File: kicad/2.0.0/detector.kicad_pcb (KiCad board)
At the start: 2 copper layers, 67 parts, among them U1 LM317, U2 LM337, U3 REF5010ID, U4 OPA2197xD, U5 OPA2197xD

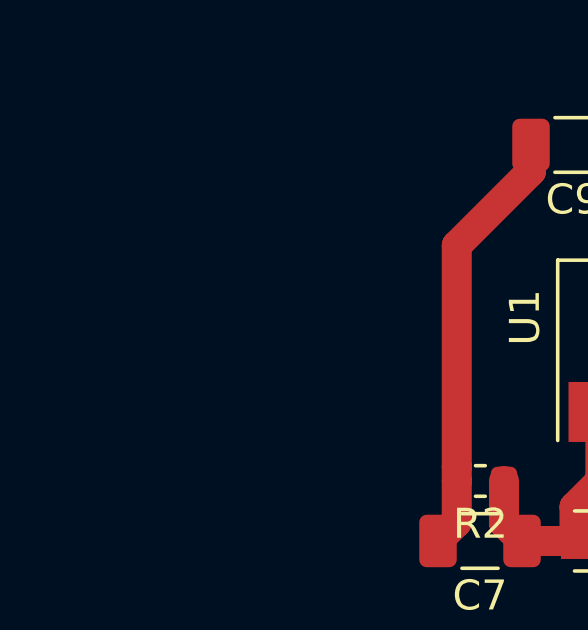
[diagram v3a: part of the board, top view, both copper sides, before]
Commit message: replaced voltage regulators of 2.0.0 detector with LDO regulators
Low-dropout (LDO) voltage regulators come in small packages, i.e.
SOT-23, however they are more susceptible for ringing.
The packages in which you can buy the non-LDO voltage regulators, e.g. SOIC-8 or SOT-223,
are large compared to the remaining circuitry.
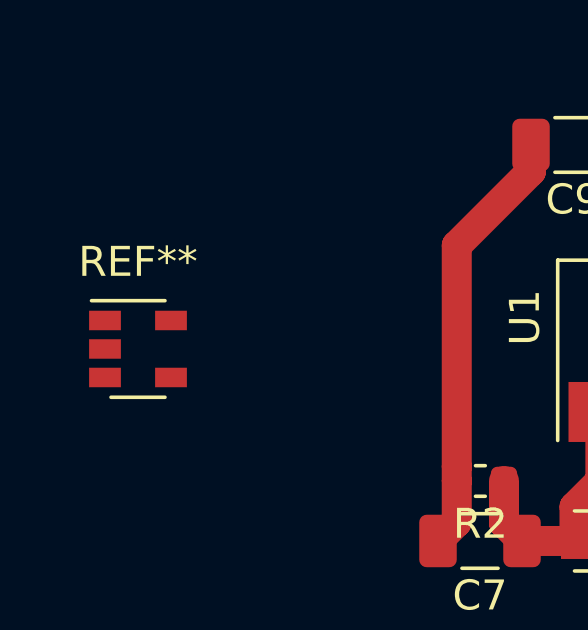
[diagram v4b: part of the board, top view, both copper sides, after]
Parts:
- added REF**: SOT-23-5, Package_TO_SOT_SMD:SOT-23-5, F.Cu at (44.3, 88.2)
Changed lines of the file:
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@@
     (tracks 155)
     (zones 0)
-    (modules 67)
+    (modules 68)
     (nets 25)
   )
@@
     (35 F.Paste user)
     (36 B.SilkS user)
-    (37 F.SilkS user hide)
+    (37 F.SilkS user)
     (38 B.Mask user)
     (39 F.Mask user)
@@
     (47 F.CrtYd user)
     (48 B.Fab user)
-    (49 F.Fab user hide)
+    (49 F.Fab user)
   )
   (setup
@@
     (add_net "Net-(U3-Pad8)")
   )
+  (module Package_TO_SOT_SMD:SOT-23-5 (layer F.Cu)
+    (at 44.3 88.2)
+    (descr "5-pin SOT23 package")
+    (tags SOT-23-5)
+    (attr smd)
+    (fp_text reference REF** (at 0 -2.9) (layer F.SilkS)
+      (effects (font (size 1 1) (thickness 0.15)))
+    )
+    (fp_text value SOT-23-5 (at 0 2.9) (layer F.Fab)
+      (effects (font (size 1 1) (thickness 0.15)))
+    )
+    (fp_line (start 0.9 -1.55) (end 0.9 1.55) (layer F.Fab) (width 0.1))
+    (fp_line (start 0.9 1.55) (end -0.9 1.55) (layer F.Fab) (width 0.1))
+    (fp_line (start -0.9 -0.9) (end -0.9 1.55) (layer F.Fab) (width 0.1))
+    (fp_line (start 0.9 -1.55) (end -0.25 -1.55) (layer F.Fab) (width 0.1))
+    (fp_line (start -0.9 -0.9) (end -0.25 -1.55) (layer F.Fab) (width 0.1))
+    (fp_line (start -1.9 1.8) (end -1.9 -1.8) (layer F.CrtYd) (width 0.05))
+    (fp_line (start 1.9 1.8) (end -1.9 1.8) (layer F.CrtYd) (width 0.05))
+    (fp_line (start 1.9 -1.8) (end 1.9 1.8) (layer F.CrtYd) (width 0.05))
+    (fp_line (start -1.9 -1.8) (end 1.9 -1.8) (layer F.CrtYd) (width 0.05))
+    (fp_line (start 0.9 -1.61) (end -1.55 -1.61) (layer F.SilkS) (width 0.12))
+    (fp_line (start -0.9 1.61) (end 0.9 1.61) (layer F.SilkS) (width 0.12))
+    (fp_text user %R (at 0 0 90) (layer F.Fab)
+      (effects (font (size 0.5 0.5) (thickness 0.075)))
+    )
+    (pad 5 smd rect (at 1.1 -0.95) (size 1.06 0.65) (layers F.Cu F.Paste F.Mask))
+    (pad 4 smd rect (at 1.1 0.95) (size 1.06 0.65) (layers F.Cu F.Paste F.Mask))
+    (pad 3 smd rect (at -1.1 0.95) (size 1.06 0.65) (layers F.Cu F.Paste F.Mask))
+    (pad 2 smd rect (at -1.1 0) (size 1.06 0.65) (layers F.Cu F.Paste F.Mask))
+    (pad 1 smd rect (at -1.1 -0.95) (size 1.06 0.65) (layers F.Cu F.Paste F.Mask))
+    (model ${KISYS3DMOD}/Package_TO_SOT_SMD.3dshapes/SOT-23-5.wrl
+      (at (xyz 0 0 0))
+      (scale (xyz 1 1 1))
+      (rotate (xyz 0 0 0))
+    )
+  )
   (module Capacitor_SMD:C_0603_1608Metric (layer F.Cu)

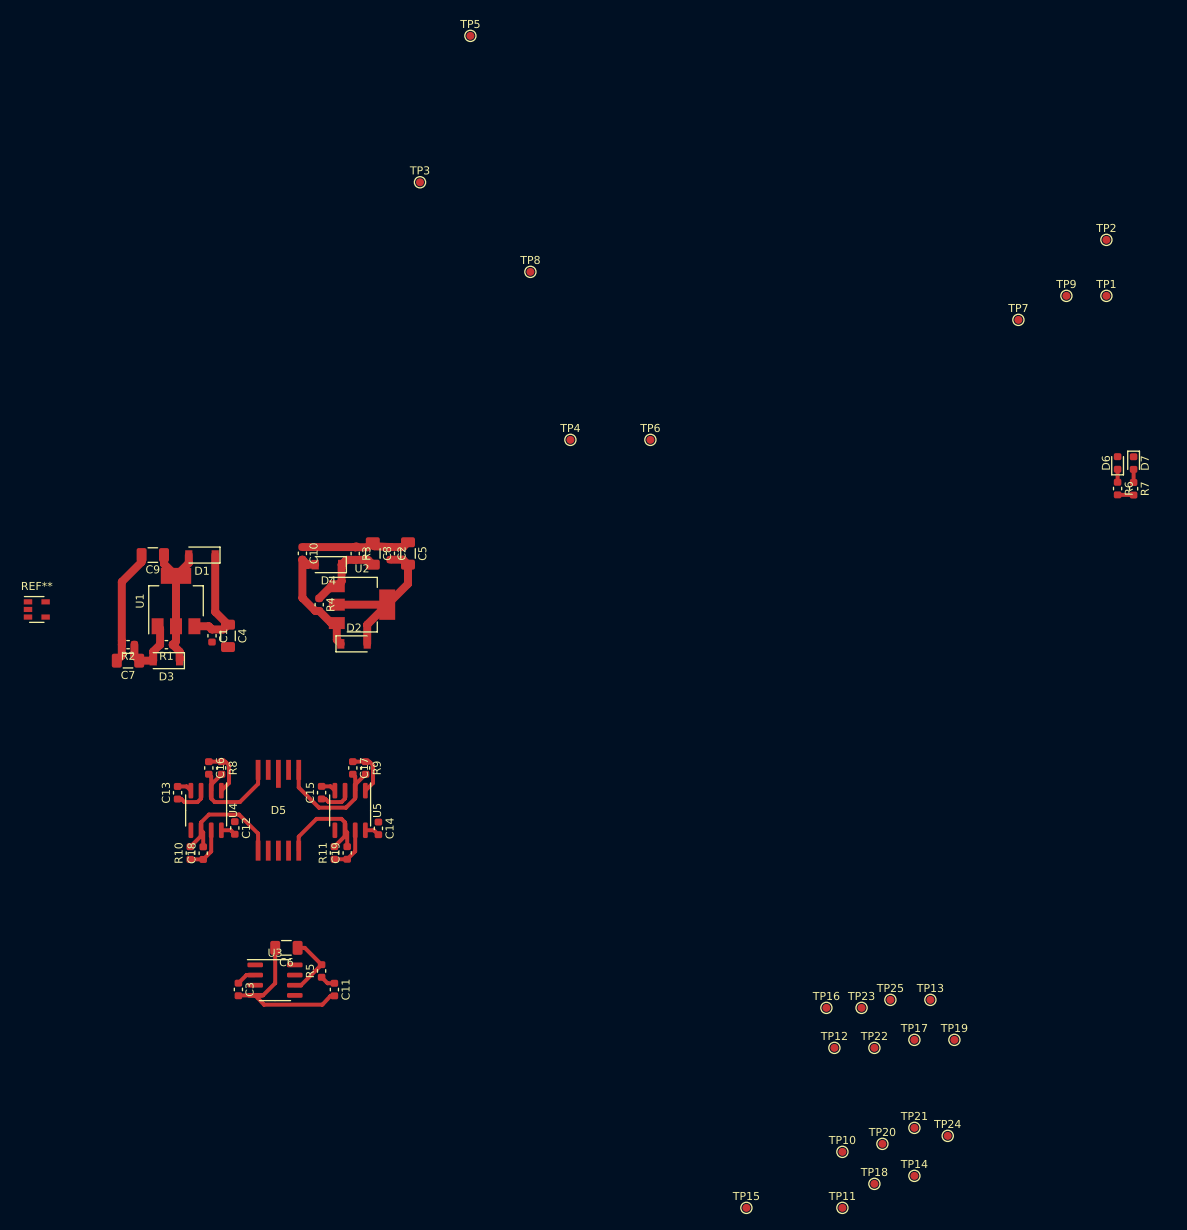
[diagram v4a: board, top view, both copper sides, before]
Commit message: updated pcb of 2.0.0 detector with new power supply
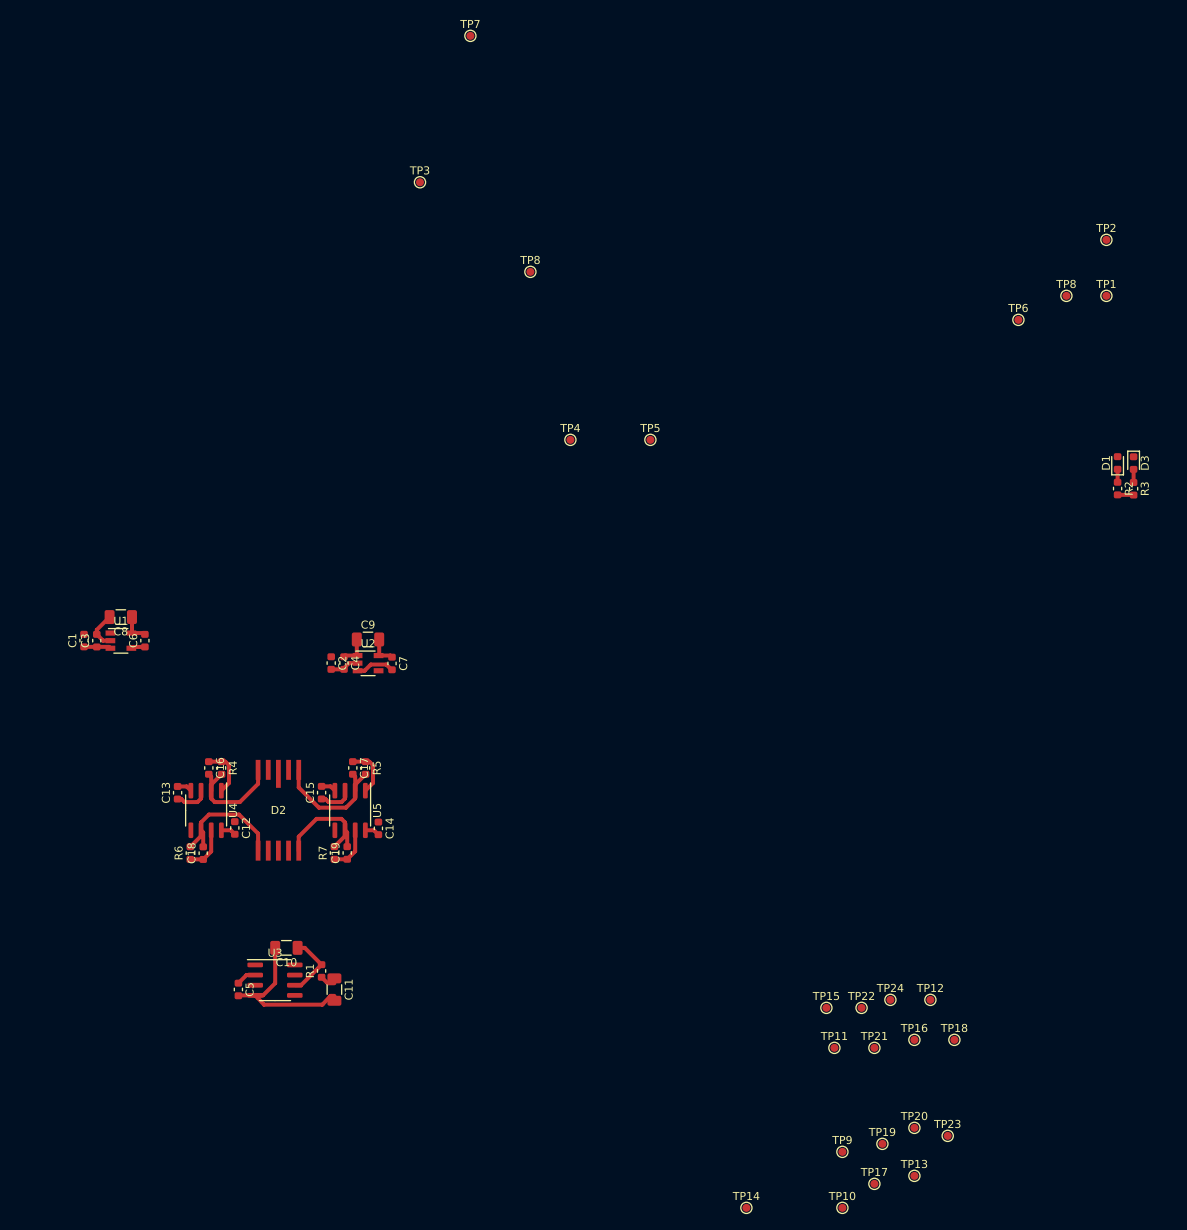
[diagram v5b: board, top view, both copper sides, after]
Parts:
- removed the C10 at (77.5, 81.2)
- removed the C5 at (90.7, 81.2)
- removed the D1 at (65.0, 81.4)
- removed the D2 at (84.0, 92.5)
- removed the D3 at (60.5, 94.6)
- removed D4: D_Small, Diode_SMD:D_SOD-123
- removed the R1 at (60.5, 92.6)
- removed the R2 at (55.7, 92.6)
- removed the R3 at (84.1, 81.2)
- removed the R4 at (79.6, 87.6)
- removed REF**: SOT-23-5, Package_TO_SOT_SMD:SOT-23-5
- added C3: 1u, Capacitor_SMD:C_0603_1608Metric, F.Cu at (51.8, 92.1)
- added C6: 10n, Capacitor_SMD:C_0603_1608Metric, F.Cu at (57.8, 92.1)
- C1, C2: value 10u -> 100n
- C11: footprint Capacitor_SMD:C_0603_1608Metric -> Capacitor_SMD:C_1206_3216Metric
- C4: value 100n -> 1u; footprint Capacitor_SMD:C_1206_3216Metric -> Capacitor_SMD:C_0603_1608Metric
- C7: value 10u -> 10n; footprint Capacitor_SMD:C_1206_3216Metric -> Capacitor_SMD:C_0603_1608Metric
- C8: value 10u -> 22u
- U1: value LM317 -> LT1761-5; footprint Package_TO_SOT_SMD:SOT-223-3_TabPin2 -> Package_TO_SOT_SMD:TSOT-23-5
- U2: value LM337 -> LT1964-5; footprint Package_TO_SOT_SMD:SOT-223-3_TabPin2 -> Package_TO_SOT_SMD:TSOT-23-5
- moved C7 33.0 mm to (88.7, 95.0), turned to 270 degrees
- moved C8 32.5 mm to (54.8, 89.2), turned to 180 degrees
- moved C9 28.9 mm to (85.7, 92.0), turned to 0 degrees
- moved C1 16.0 mm to (50.2, 92.1), turned to 90 degrees
- moved C2 15.6 mm to (81.1, 94.9)
- moved C4 14.9 mm to (82.7, 94.9)
- moved U1 8.48 mm to (54.8, 92.1), turned to 0 degrees
- moved U2 7.35 mm to (85.7, 94.9)
- renumbered C6 to C10, C3 to C5, D6 to D1, D5 to D2, D7 to D3, R5 to R1, R6 to R2, R7 to R3, R8 to R4, R9 to R5, R10 to R6, R11 to R7, TP11 to TP10, TP12 to TP11, TP13 to TP12, TP14 to TP13, TP15 to TP14, TP16 to TP15, TP17 to TP16, TP18 to TP17, TP19 to TP18, TP20 to TP19, TP21 to TP20, TP22 to TP21, TP23 to TP22, TP24 to TP23, TP25 to TP24, TP6 to TP5, TP7 to TP6, TP5 to TP7, TP9 to TP8, TP10 to TP9
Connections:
- C1 pad 2: GND -> Net-(C1-Pad2)
- C2 pad 1: GND -> Net-(C1-Pad2)
- C4 pad 1: +15V -> GND
- C4 pad 2: GND -> -15V
- C7 pad 1: Net-(C7-Pad1) -> -5V
- C7 pad 2: GND -> Net-(C7-Pad2)
- C8 pad 1: GND -> +5V
- C8 pad 2: Net-(C8-Pad2) -> GND
- C9 pad 1: +12V -> GND
- C9 pad 2: GND -> -5V
- TP5 pad 1: +12V -> +5V
- TP6 pad 1: -12V -> -5V
- U1 pad 1: Net-(C7-Pad1) -> +15V
- U1 pad 2: +12V -> GND
- U2 pad 1: Net-(C8-Pad2) -> GND
- U2 pad 3: -12V -> Net-(C7-Pad2)
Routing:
- net GND: track 59.8 -> 39.7 mm
- net +12V: track 23.9 -> 6.26 mm
- net -15V: track 20.8 -> 3.62 mm
- net -12V: track 18.8 -> 3.76 mm
- net +15V: track 14.0 -> 3.37 mm
- net Net-(C8-Pad2): track 10.2 -> 0.00 mm
- net Net-(C7-Pad1): track 8.79 -> 0.00 mm
- net Net-(C7-Pad2): track 0.00 -> 4.97 mm
- net -5V: track 0.00 -> 3.81 mm
- net +5V: track 0.00 -> 3.79 mm
- net Net-(C6-Pad1): track 0.00 -> 1.76 mm

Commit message: placed testpoints on pcb for 2.0.0 detector
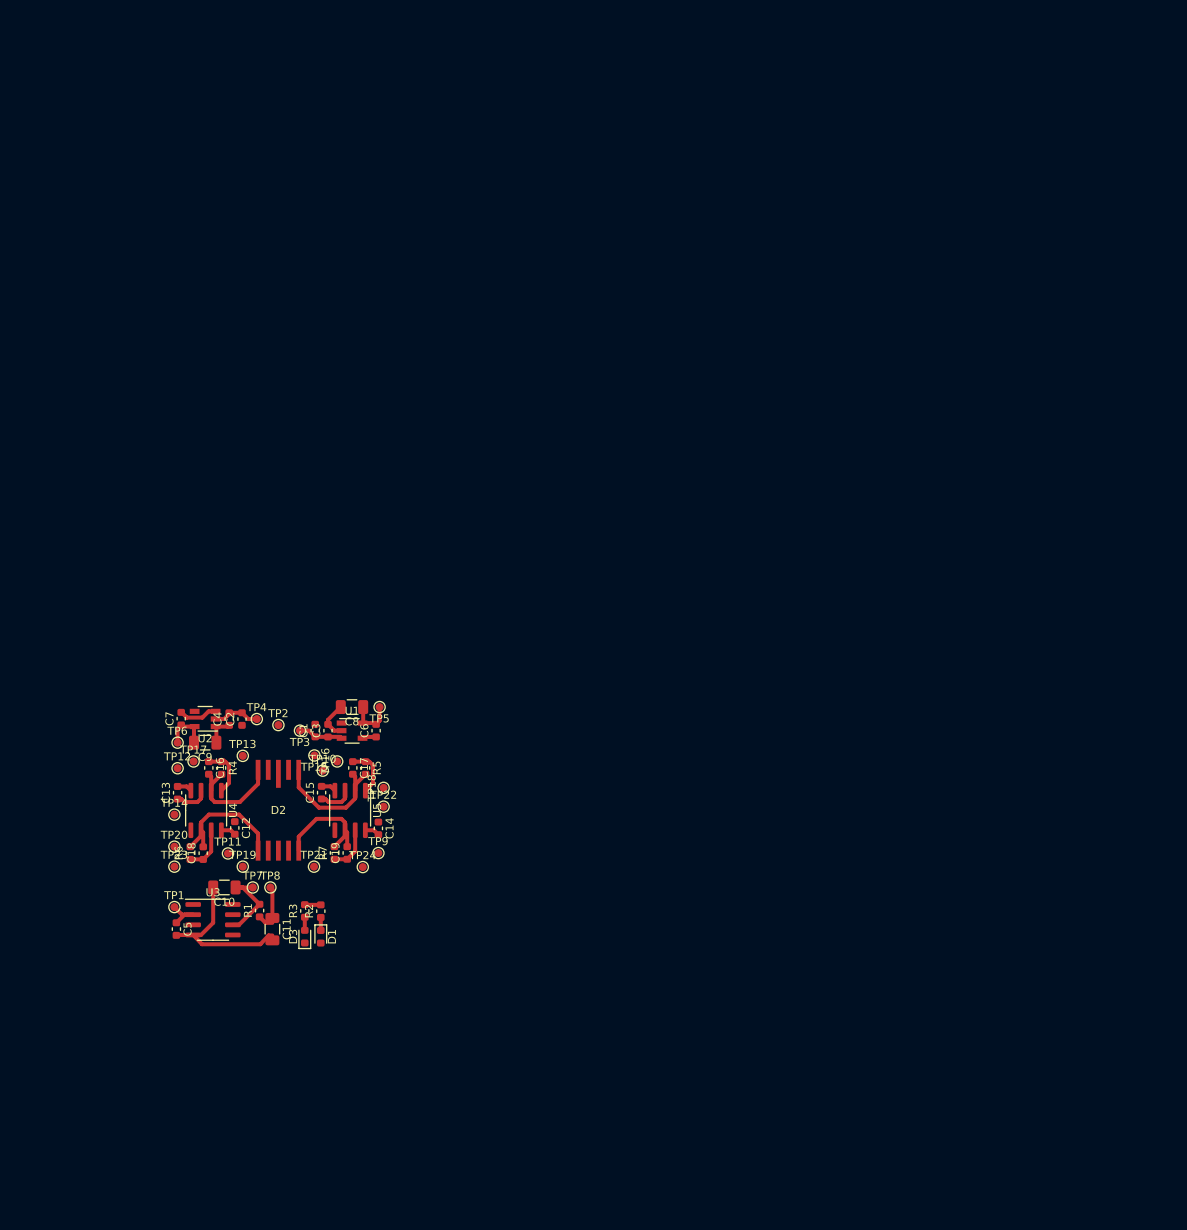
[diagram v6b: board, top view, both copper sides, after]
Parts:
- removed the TP8 at (106.0, 46.0)
- removed the TP8 at (173.0, 49.0)
- added TP8: BIAS, TestPoint:TestPoint_Pad_D1.0mm, F.Cu at (73.5, 123.0)
- R2: value 510 -> 130
- R3: value 550 -> 160
- TP1: value +12V -> +15V
- TP10, TP12, TP6: value -12V -> -5V
- TP11, TP5, TP9: value +12V -> +5V
- moved TP1 139.3 mm to (61.5, 125.4)
- moved TP2 120.0 mm to (74.5, 102.7)
- moved D3 119.3 mm to (77.8, 129.1), turned to 90 degrees
- moved TP6 117.6 mm to (61.9, 104.8)
- moved R3 116.3 mm to (77.8, 125.9), turned to 90 degrees
- moved D1 115.9 mm to (79.8, 129.1), turned to 270 degrees
- moved R2 112.7 mm to (79.8, 125.9), turned to 90 degrees
- moved TP7 109.9 mm to (71.3, 123.0)
- moved TP23 102.4 mm to (61.5, 120.3)
- moved TP17 100.1 mm to (63.9, 107.2)
- moved TP13 99.0 mm to (70.0, 106.5)
- moved TP20 99.0 mm to (61.5, 117.8)
- moved TP12 98.5 mm to (61.9, 108.0)
- moved TP19 87.1 mm to (70.0, 120.3)
- moved TP14 86.8 mm to (61.5, 113.8)
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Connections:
- C12 pad 2: +12V -> +5V
- C13 pad 2: -12V -> -5V
- C14 pad 2: +12V -> +5V
- C15 pad 2: -12V -> -5V
- C5 pad 1: +12V -> +15V
- D1 pad 2: +12V -> +5V
- D3 pad 1: -12V -> -5V
- TP1 pad 1: +12V -> +15V
- TP10 pad 1: -12V -> -5V
- TP11 pad 1: +12V -> +5V
- TP12 pad 1: -12V -> -5V
- TP9 pad 1: +12V -> +5V
- U3 pad 2: +12V -> +15V
- U4 pad 4: -12V -> -5V
- U4 pad 8: +12V -> +5V
- U5 pad 4: -12V -> -5V
- U5 pad 8: +12V -> +5V
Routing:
- net +15V: track 3.37 -> 10.9 mm
- net -5V: track 3.81 -> 10.2 mm
- net +12V: track 6.26 -> 0.00 mm
- net +5V: track 3.79 -> 9.88 mm
- net Net-(C11-Pad1): track 1.91 -> 5.83 mm
- net -12V: track 3.76 -> 0.00 mm
- net -15V: track 3.62 -> 5.80 mm
- net Net-(C10-Pad1): track 8.28 -> 10.4 mm
